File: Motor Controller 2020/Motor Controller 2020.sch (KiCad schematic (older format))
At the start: 48 parts, among them J1 Batt+, J2 Batt-, J3 Input, J4 Motor+, J5 Motor-, Q1 IRF1404, Q2 IRF1404, Q3 IRF1404, Q4 IRF1404, Q5 IRF1404, Q6 IRF1404, Q7 IRF1404, Q8 IRF1404, SW1 SW_DIP_x03, U1 MAX15062A, U2 a4956, U3 Attiny4313

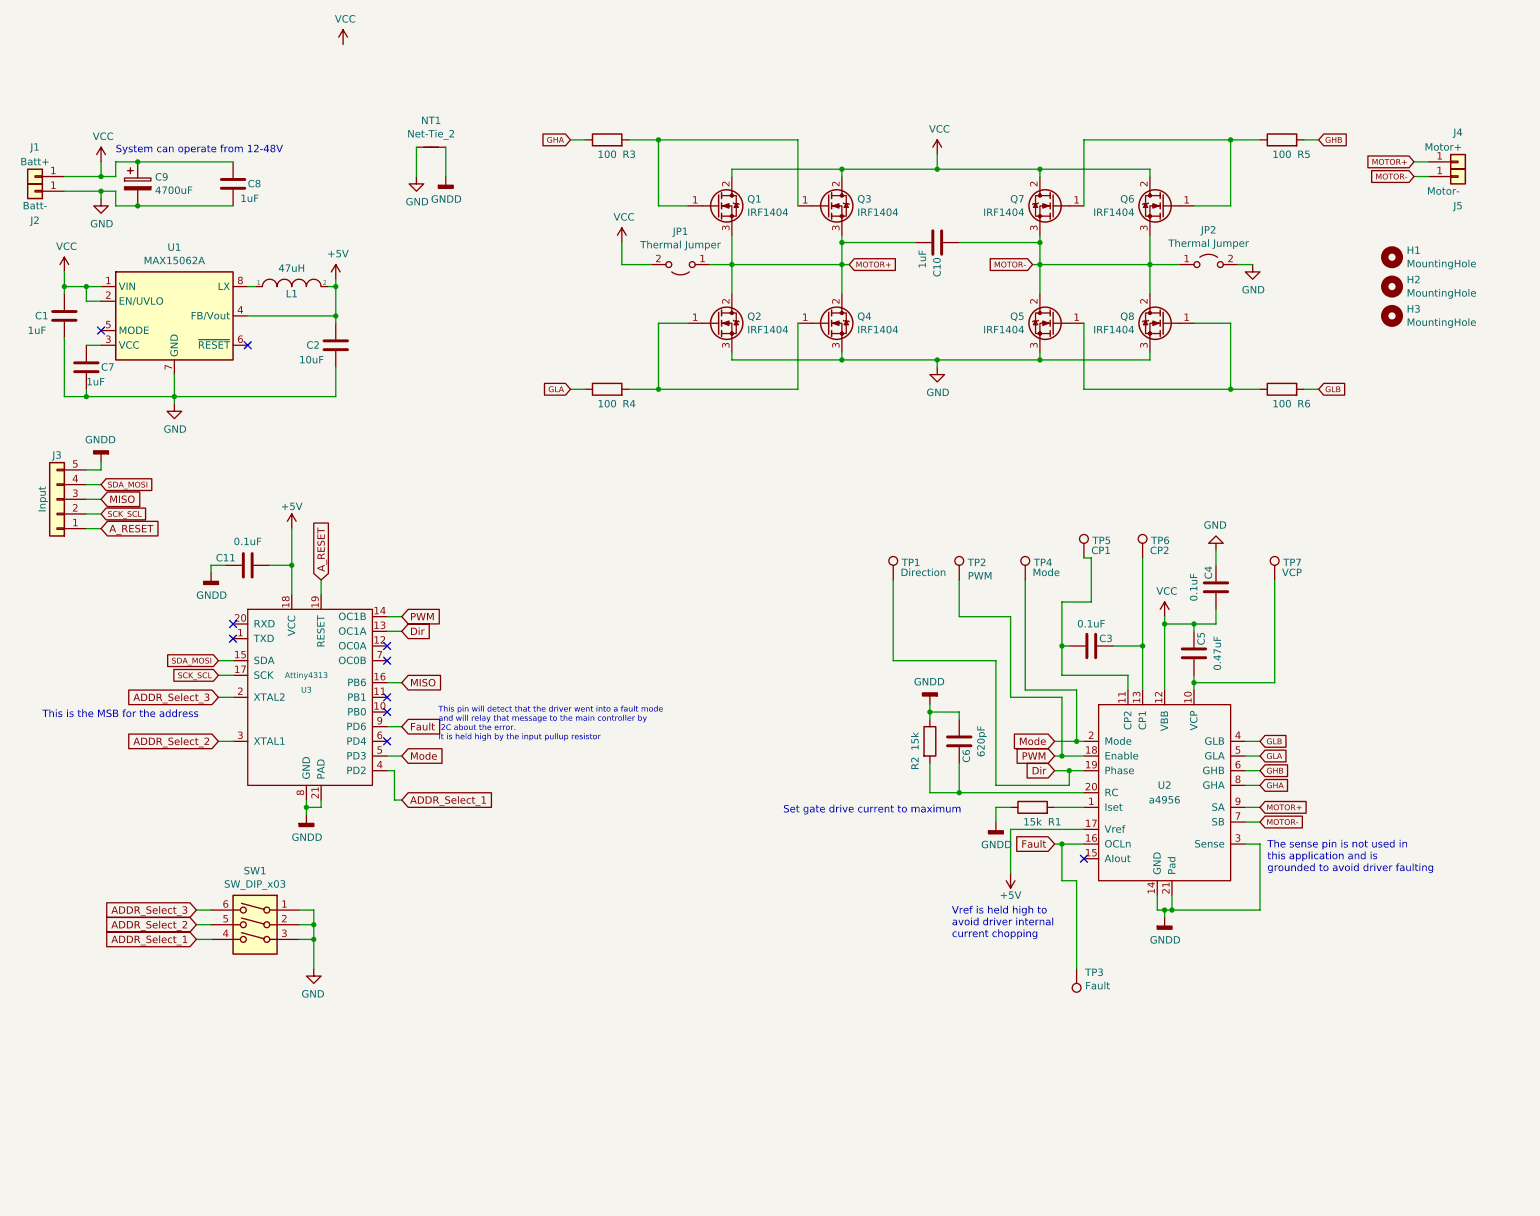
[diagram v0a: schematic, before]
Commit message: Re-arranged components
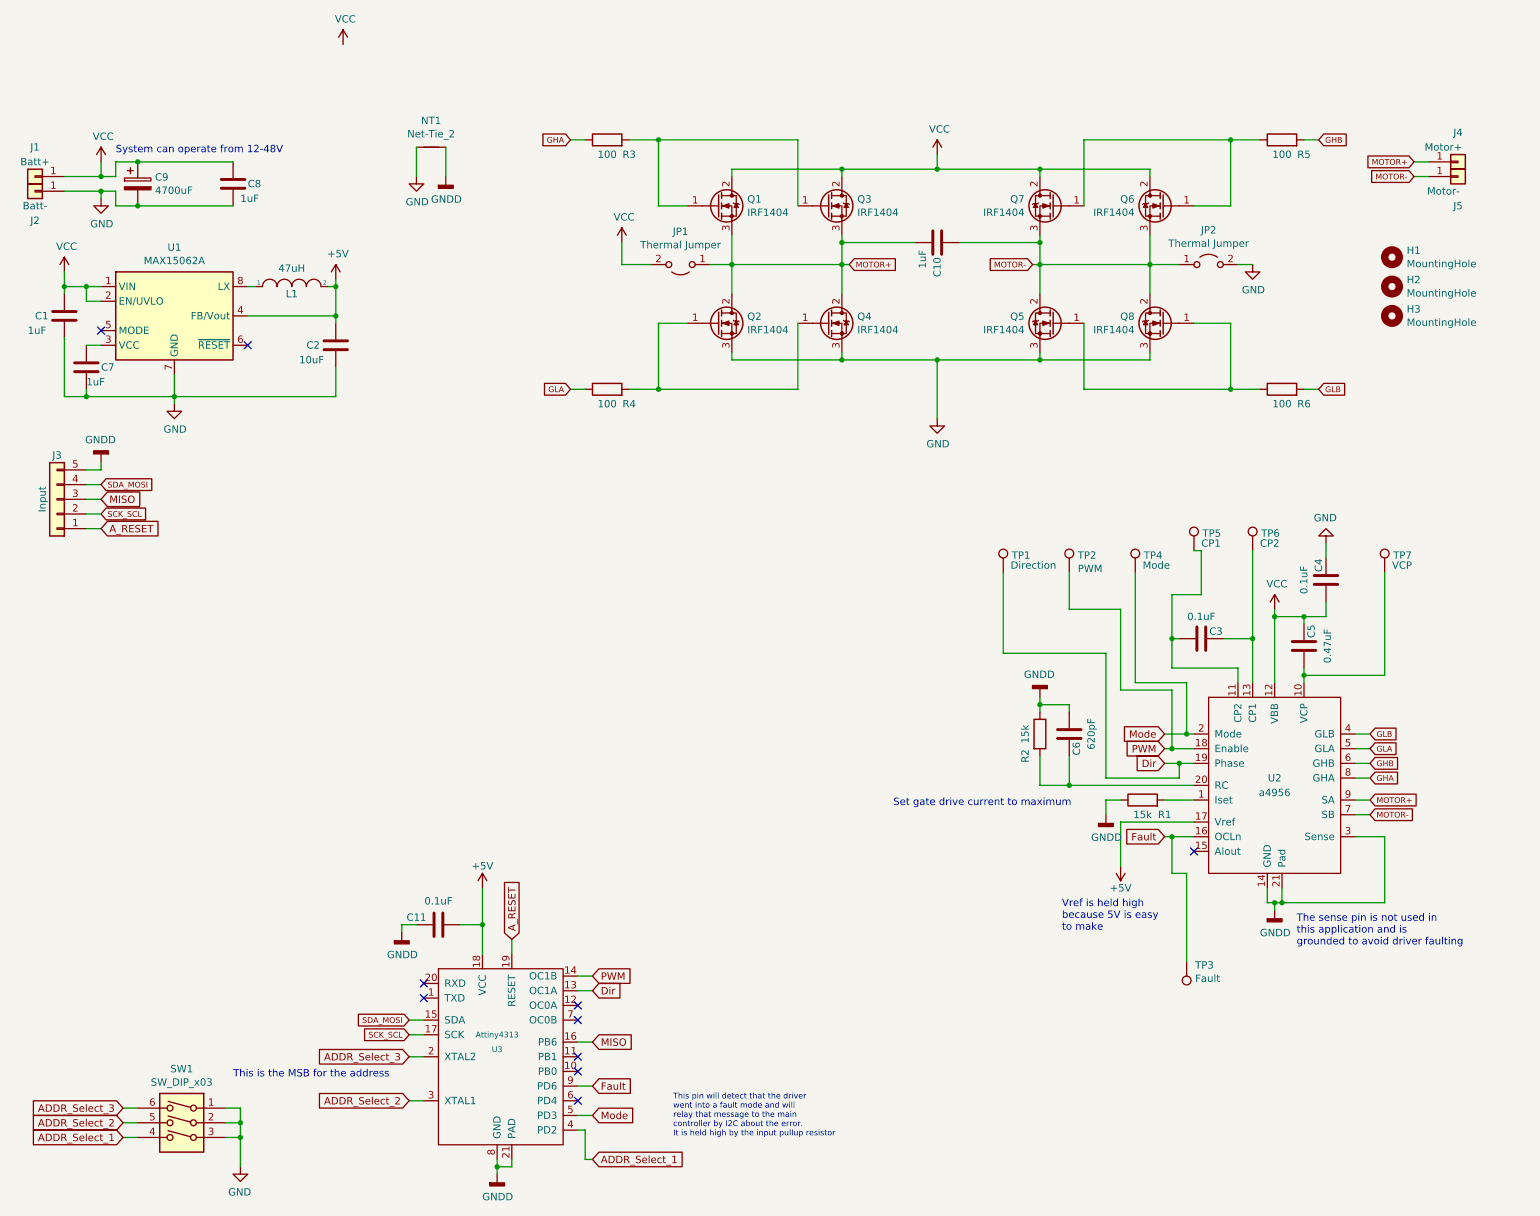
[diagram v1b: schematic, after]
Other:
- note added: "This pin will detect that the driver \nwent into a fault mode and will \nrelay that message to the main \ncontroller by I2C about the error.\nIt is held high by the input pullup resistor"
- note added: "Vref is held high \nbecause 5V is easy \nto make"
- note removed: "This pin will detect that the driver went into a fault mode \nand will relay that message to the main controller by \nI2C about the error.\nIt is held high by the input pullup resistor"
- note removed: "Vref is held high to \navoid driver internal \ncurrent chopping"
- moved on the sheet: C11, C3, C4, C5, C6, R1, R2, SW1, TP1, TP2, TP3, TP4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

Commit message: Updated PCB
Added larger caps for local storage. Also removed 4 MOSFETS because I don't believe I will need them. This will be tested when the system works properly
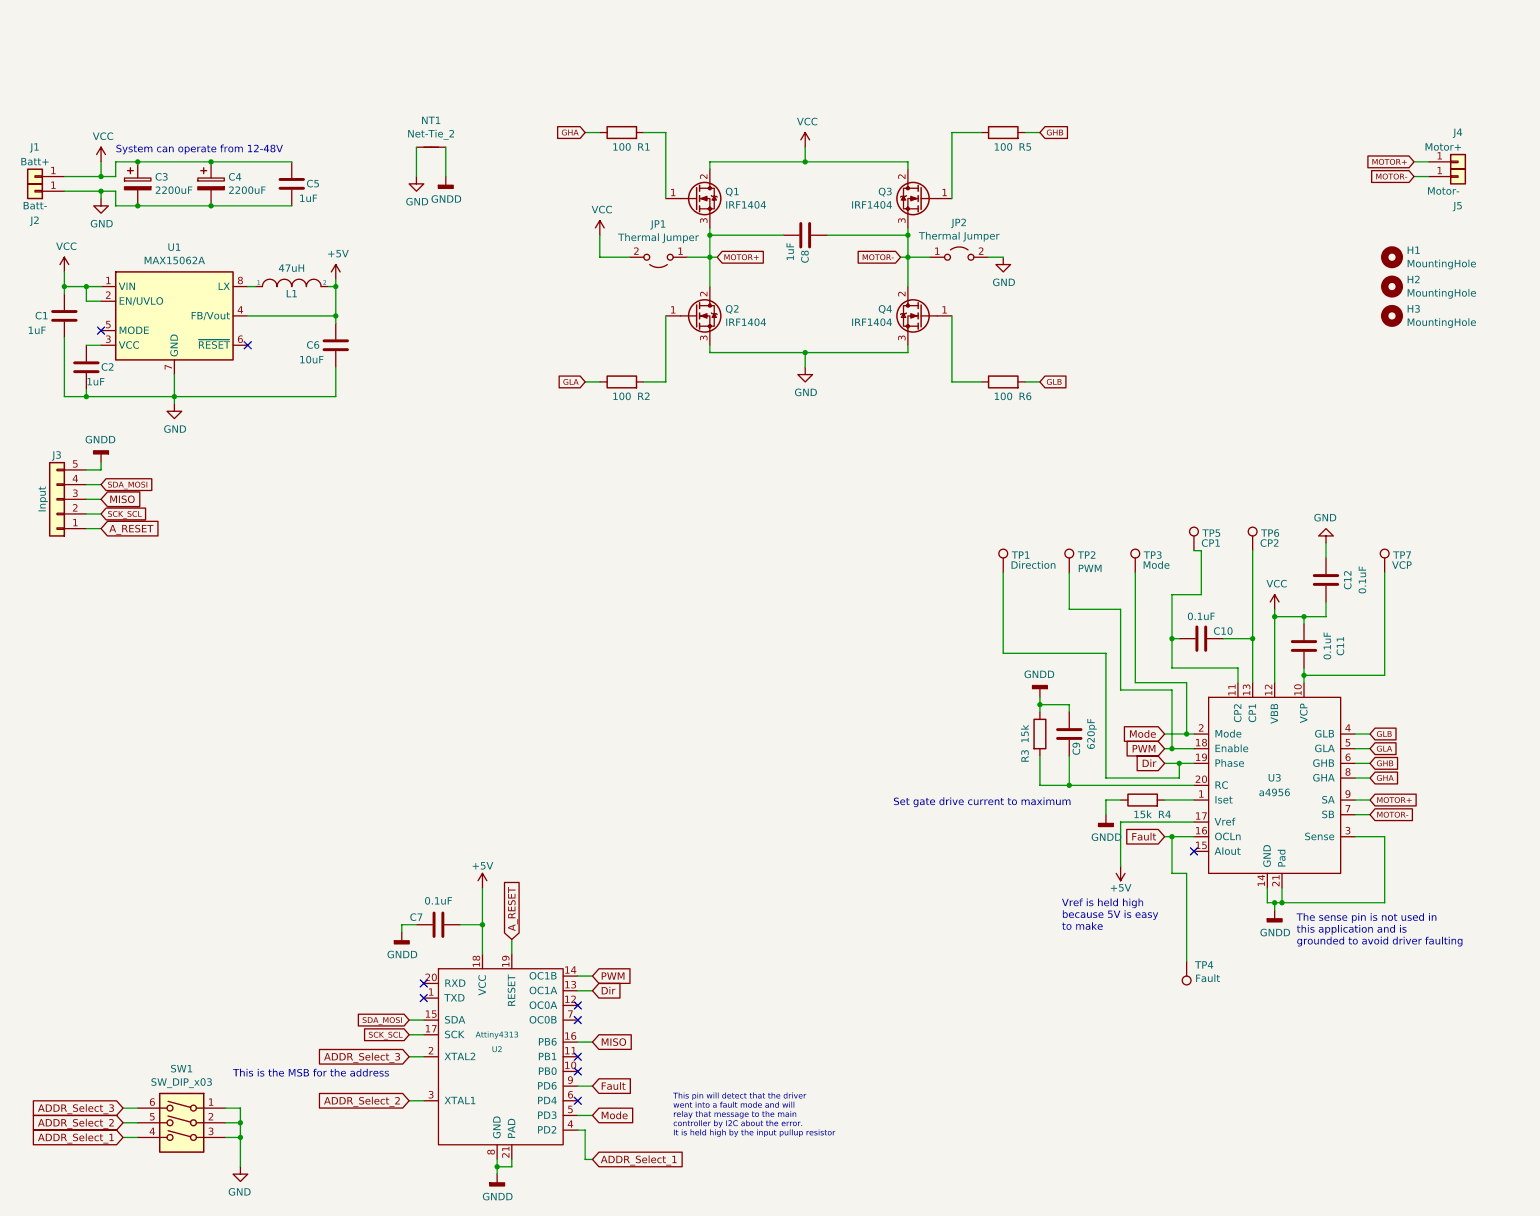
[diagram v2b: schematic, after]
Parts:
- removed Q1, Q2, Q6, Q8: IRF1404, Package_TO_SOT_SMD:TO-263-2, symbol Transistor_FET:IRF3205
- added C4: 2200uF, Capacitor_THT:C_Radial_D18.0mm_H35.5mm_P7.50mm, symbol Device:CP
- C11: renamed from C5; value 0.47uF -> 0.1uF
- C3: renamed from C9; value 4700uF -> 2200uF; footprint Capacitor_SMD:CP_Elec_18x17.5 -> Capacitor_THT:C_Radial_D18.0mm_H35.5mm_P7.50mm
- renumbered C3 to C10, C4 to C12, C7 to C2, C8 to C5, C2 to C6, C11 to C7, C10 to C8, C6 to C9, Q3 to Q1, Q4 to Q2, Q7 to Q3, Q5 to Q4, R3 to R1, R4 to R2, R2 to R3, R1 to R4, TP4 to TP3, TP3 to TP4, U3 to U2, U2 to U3
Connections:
- net GND: now also C4.2
- net VCC: now also C4.1
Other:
- moved on the sheet: C5, C8, JP1, JP2, Q1, Q2, Q3, Q4, R1, R2, R5, R6

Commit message: Add files via upload
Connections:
- net GND: now also C9.2, R3.1, R4.1, U3.14 (GND), U3.21 (Pad), U3.3 (Sense)
- net GNDD: no longer C9.2, R3.1, R4.1, U3.14 (GND), U3.21 (Pad), U3.3 (Sense)
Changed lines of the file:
@@
-$EndComp
-$Comp
-L power:GNDD #PWR021
-U 1 1 60E43F9D
-P 9050 5900
-F 0 "#PWR021" H 9050 5650 50  0001 C CNN
-F 1 "GNDD" H 9054 5745 50  0000 C CNN
-F 2 "" H 9050 5900 50  0001 C CNN
-F 3 "" H 9050 5900 50  0001 C CNN
-	1    9050 5900
-	1    0    0    -1
-$EndComp
-$Comp
-L power:GNDD #PWR017
-U 1 1 60E45DA5
-P 7900 5250
-F 0 "#PWR017" H 7900 5000 50  0001 C CNN
-F 1 "GNDD" H 7904 5095 50  0000 C CNN
-F 2 "" H 7900 5250 50  0001 C CNN
-F 3 "" H 7900 5250 50  0001 C CNN
-	1    7900 5250
-	1    0    0    -1
-$EndComp
-$Comp
-L power:GNDD #PWR016
-U 1 1 60E876F0
-P 7450 4450
-F 0 "#PWR016" H 7450 4200 50  0001 C CNN
-F 1 "GNDD" H 7454 4295 50  0000 C CNN
-F 2 "" H 7450 4450 50  0001 C CNN
-F 3 "" H 7450 4450 50  0001 C CNN
-	1    7450 4450
-	-1   0    0    1
 $EndComp
 $Comp
@@
 Wire Wire Line
 	5850 2100 5850 2200
+$Comp
+L power:GND #PWR?
+U 1 1 60E68E05
+P 9050 5900
+F 0 "#PWR?" H 9050 5650 50  0001 C CNN
+F 1 "GND" H 9055 5727 50  0000 C CNN
+F 2 "" H 9050 5900 50  0001 C CNN
+F 3 "" H 9050 5900 50  0001 C CNN
+	1    9050 5900
+	1    0    0    -1
+$EndComp
+$Comp
+L power:GND #PWR?
+U 1 1 60E69559
+P 7900 5250
+F 0 "#PWR?" H 7900 5000 50  0001 C CNN
+F 1 "GND" H 7905 5077 50  0000 C CNN
+F 2 "" H 7900 5250 50  0001 C CNN
+F 3 "" H 7900 5250 50  0001 C CNN
+	1    7900 5250
+	1    0    0    -1
+$EndComp
+$Comp
+L power:GND #PWR?
+U 1 1 60E69A5E
+P 7450 4450
+F 0 "#PWR?" H 7450 4200 50  0001 C CNN
+F 1 "GND" H 7455 4277 50  0000 C CNN
+F 2 "" H 7450 4450 50  0001 C CNN
+F 3 "" H 7450 4450 50  0001 C CNN
+	1    7450 4450
+	-1   0    0    1
+$EndComp
 $EndSCHEMATC

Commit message: Made gerber files
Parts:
- C6: value 10uF -> 22uF
- L1: value 47uH -> 68uH
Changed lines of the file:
@@
 P 2650 2050
 F 0 "C6" H 2450 2050 50  0000 L CNN
-F 1 "10uF" H 2400 1950 50  0000 L CNN
+F 1 "22uF" H 2400 1950 50  0000 L CNN
 F 2 "Capacitor_SMD:C_1210_3225Metric" H 2688 1900 50  0001 C CNN
 F 3 "~" H 2650 2050 50  0001 C CNN
@@
 P 2350 1650
 F 0 "L1" H 2350 1600 50  0000 C CNN
-F 1 "47uH" H 2350 1774 50  0000 C CNN
+F 1 "68uH" H 2350 1774 50  0000 C CNN
 F 2 "Inductor_SMD:L_1210_3225Metric" H 2350 1650 50  0001 C CNN
 F 3 "~" H 2350 1650 50  0001 C CNN

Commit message: Added status lights
Added power and status lights to help diagnose issues when the system is running without screen on the master controller
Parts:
- added D1: Power On, LED_SMD:LED_1206_3216Metric, symbol Device:LED
- added D2: Status LED, Motor Controller 2020:LED_0603_4_pin, symbol Device:LED_Dual_CACA
- added R7, R8: 150, Resistor_SMD:R_1206_3216Metric, symbol Device:R
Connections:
- net +5V: now also D1.2 (A)
- net GND: now also R7.2, R8.2
- net at U2.1 (TXD): now also D2.4 (K2)
- net at U2.20 (RXD): now also D2.2 (K1)
- new net: D1.1 (K), R7.1
- new net: D2.1 (A1), D2.3 (A2), R8.1
- no-connect marks 10 -> 8
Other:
- note added: "RED"
- note added: "YLW"
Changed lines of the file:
@@
 NoConn ~ 4300 7000
 NoConn ~ 4300 7200
-NoConn ~ 3250 6400
-NoConn ~ 3250 6500
 $Comp
 L Transistor_FET:IRF3205 Q1
@@
 	5850 2100 5850 2200
 $Comp
-L power:GND #PWR?
+L power:GND #PWR021
 U 1 1 60E68E05
 P 9050 5900
-F 0 "#PWR?" H 9050 5650 50  0001 C CNN
+F 0 "#PWR021" H 9050 5650 50  0001 C CNN
 F 1 "GND" H 9055 5727 50  0000 C CNN
 F 2 "" H 9050 5900 50  0001 C CNN
@@
 $EndComp
 $Comp
-L power:GND #PWR?
+L power:GND #PWR017
 U 1 1 60E69559
 P 7900 5250
-F 0 "#PWR?" H 7900 5000 50  0001 C CNN
+F 0 "#PWR017" H 7900 5000 50  0001 C CNN
 F 1 "GND" H 7905 5077 50  0000 C CNN
 F 2 "" H 7900 5250 50  0001 C CNN
@@
 $EndComp
 $Comp
-L power:GND #PWR?
+L power:GND #PWR016
 U 1 1 60E69A5E
 P 7450 4450
-F 0 "#PWR?" H 7450 4200 50  0001 C CNN
+F 0 "#PWR016" H 7450 4200 50  0001 C CNN
 F 1 "GND" H 7455 4277 50  0000 C CNN
 F 2 "" H 7450 4450 50  0001 C CNN
@@
 	-1   0    0    1
 $EndComp
+$Comp
+L Device:LED D1
+U 1 1 610DE257
+P 3050 1800
+F 0 "D1" V 3089 1682 50  0000 R CNN
+F 1 "Power On" V 2998 1682 50  0000 R CNN
+F 2 "LED_SMD:LED_1206_3216Metric" H 3050 1800 50  0001 C CNN
+F 3 "~" H 3050 1800 50  0001 C CNN
+	1    3050 1800
+	0    -1   -1   0
+$EndComp
+Wire Wire Line
+	3050 2300 3050 2400
+Wire Wire Line
+	3050 2400 2650 2400
+Connection ~ 2650 2400
+$Comp
+L Device:R R7
+U 1 1 610E9243
+P 3050 2150
+F 0 "R7" V 2950 2000 50  0000 C CNN
+F 1 "150" V 2950 2150 50  0000 C CNN
+F 2 "Resistor_SMD:R_1206_3216Metric" V 2980 2150 50  0001 C CNN
+F 3 "~" H 3050 2150 50  0001 C CNN
+	1    3050 2150
+	1    0    0    -1
+$EndComp
+Wire Wire Line
+	3050 1650 2650 1650
+Wire Wire Line
+	3050 1950 3050 2000
+$Comp
+L Device:R R8
+U 1 1 61101F1F
+P 2000 6400
+F 0 "R8" V 1900 6250 50  0000 C CNN
+F 1 "150" V 1900 6400 50  0000 C CNN
+F 2 "Resistor_SMD:R_1206_3216Metric" V 1930 6400 50  0001 C CNN
+F 3 "~" H 2000 6400 50  0001 C CNN
+	1    2000 6400
+	0    1    1    0
+$EndComp
+$Comp
+L power:GND #PWR023
+U 1 1 61104004
+P 1750 6400
+F 0 "#PWR023" H 1750 6150 50  0001 C CNN
+F 1 "GND" H 1755 6227 50  0000 C CNN
+F 2 "" H 1750 6400 50  0001 C CNN
+F 3 "" H 1750 6400 50  0001 C CNN
+	1    1750 6400
+	0    1    1    0
+$EndComp
+Wire Wire Line
+	1750 6400 1850 6400
+Wire Wire Line
+	2150 6400 2250 6400
+Wire Wire Line
+	2850 6500 3250 6500
+Wire Wire Line
+	3250 6400 3000 6400
+Wire Wire Line
+	3000 6400 3000 6300
+Wire Wire Line
+	3000 6300 2850 6300
+$Comp
+L Device:LED_Dual_CACA D2
+U 1 1 61160014
+P 2550 6400
+F 0 "D2" H 2550 6825 50  0000 C CNN
+F 1 "Status LED" H 2550 6734 50  0000 C CNN
+F 2 "Motor Controller 2020:LED_0603_4_pin" H 2580 6400 50  0001 C CNN
+F 3 "~" H 2580 6400 50  0001 C CNN
+	1    2550 6400
+	1    0    0    -1
+$EndComp
+Wire Wire Line
+	2250 6300 2250 6400
+Wire Wire Line
+	2250 6500 2250 6400
+Connection ~ 2250 6400
+Text Notes 2500 6700 0    50   ~ 0
+YLW
+Text Notes 2500 6200 0    50   ~ 0
+RED
 $EndSCHEMATC

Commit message: Created new version
Updated PCB and added CRC check for incoming data
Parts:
- added R9: 15k, Resistor_SMD:R_1206_3216Metric, symbol Device:R
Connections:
- net +5V: now also R9.1
- net A_RESET: now also R9.2
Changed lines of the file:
@@
 	3650 5750 3650 6000
 Wire Wire Line
-	3850 6200 3850 6100
+	3850 6200 3850 6150
 $Comp
 L Mechanical:MountingHole H1
@@
 Text Notes 2500 6200 0    50   ~ 0
 RED
+$Comp
+L Device:R R9
+U 1 1 6172CADC
+P 4100 5900
+F 0 "R9" V 4000 5750 50  0000 C CNN
+F 1 "15k" V 4000 5900 50  0000 C CNN
+F 2 "Resistor_SMD:R_1206_3216Metric" V 4030 5900 50  0001 C CNN
+F 3 "~" H 4100 5900 50  0001 C CNN
+	1    4100 5900
+	1    0    0    -1
+$EndComp
+$Comp
+L power:+5V #PWR024
+U 1 1 6172D985
+P 4100 5650
+F 0 "#PWR024" H 4100 5500 50  0001 C CNN
+F 1 "+5V" H 4100 5800 50  0000 C CNN
+F 2 "" H 4100 5650 50  0001 C CNN
+F 3 "" H 4100 5650 50  0001 C CNN
+	1    4100 5650
+	1    0    0    -1
+$EndComp
+Wire Wire Line
+	4100 5650 4100 5750
+Wire Wire Line
+	4100 6050 4100 6150
+Wire Wire Line
+	4100 6150 3850 6150
+Connection ~ 3850 6150
+Wire Wire Line
+	3850 6150 3850 6100
 $EndSCHEMATC

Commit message: Updated PCB
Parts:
- added R10: 15k, Resistor_SMD:R_1206_3216Metric, symbol Device:R
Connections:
- net GND: now also R10.2
- net VCC: now also R10.1
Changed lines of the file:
@@
 Wire Wire Line
 	3850 6150 3850 6100
+$Comp
+L Device:R R10
+U 1 1 6187A4F9
+P 2700 950
+F 0 "R10" H 2770 996 50  0000 L CNN
+F 1 "15k" H 2770 905 50  0000 L CNN
+F 2 "Resistor_SMD:R_1206_3216Metric" V 2630 950 50  0001 C CNN
+F 3 "~" H 2700 950 50  0001 C CNN
+	1    2700 950
+	1    0    0    -1
+$EndComp
+Wire Wire Line
+	2700 800  2350 800
+Connection ~ 2350 800
+Wire Wire Line
+	2700 1100 2350 1100
+Connection ~ 2350 1100
 $EndSCHEMATC
